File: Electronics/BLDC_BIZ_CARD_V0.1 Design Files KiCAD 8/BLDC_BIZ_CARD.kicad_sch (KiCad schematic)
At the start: 82 parts, among them J1 BATTERY, J11 A1+, J12 A1-, J13 A2+, J14 A2-, J15 B1+, J16 B1-, J17 B2+, J18 B2-, J19 C1+, J2 Conn_01x06_SERIAL_PROG_HEADER, J20 C1-, J21 C2+, J22 C2-, J4 Conn_01x04, J5 Conn_02x03_Odd_Even_ISP, J6 Conn_01x02_MOTOR_POWER, J8 Conn_01x03, J9 Conn_01x04, Q1 Q_PMOS_GSD, Q2 Q_NMOS_GSD, Q21 Q_PMOS_GSD, Q3 Q_PMOS_GSD, Q4 Q_NMOS_GSD, Q5 Q_PMOS_GSD, Q6 Q_NMOS_GSD, SW1 SK12D07L4B, U1 ATmega328PB-A, X1 SAO_Header, X2 QWIIC, Y1 20MHz 15pF Resonator

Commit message: Rotate ISP port on schematic to match board orientation.
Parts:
- J2: value Conn_01x06_SERIAL_PROG_HEADER -> Conn_01x06_SER_PROG
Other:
- note added: "AVR ISP PROGRAM"
- note added: "KEY AT PIN 3 KEY AT TOP FRONT SIDE OF PCB"
- note removed: "ISP PROGRAM"
- note removed: "KEY AT PIN 3"
- moved on the sheet: C5, J2, J5, J9

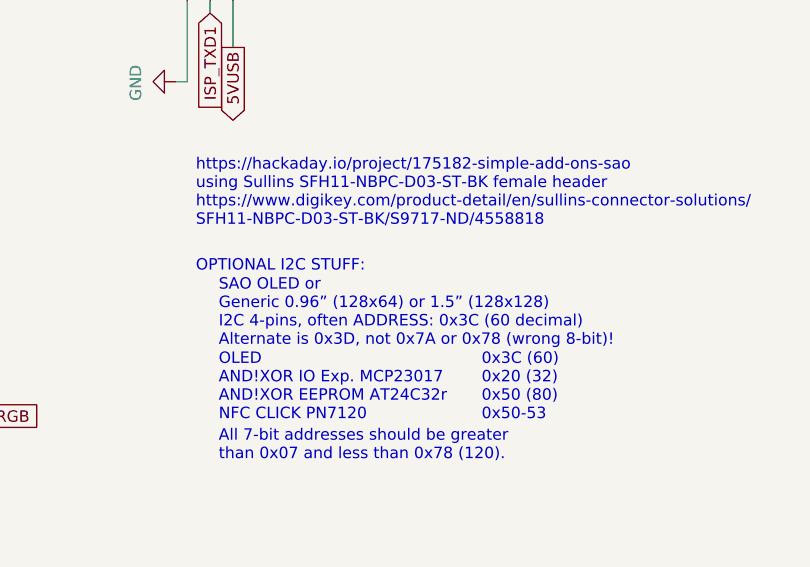
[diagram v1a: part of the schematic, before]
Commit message: Increase start-up LED color durations, add schematic OLED note
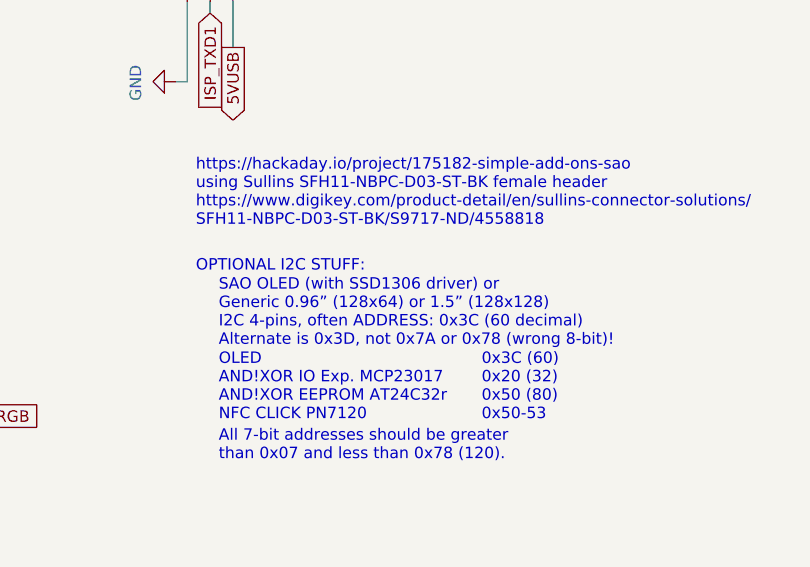
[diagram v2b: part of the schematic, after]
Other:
- note added: "SAO OLED (with SSD1306 driver) or Generic 0.96” (128x64) or 1.5” (128x128) I2C 4-pins, often ADDRESS: 0x3C (60 decimal) Alternate is 0x3D, not 0x7A or 0x78 (wrong 8-bit)!"
- note removed: "SAO OLED or Generic 0.96” (128x64) or 1.5” (128x128) I2C 4-pins, often ADDRESS: 0x3C (60 decimal) Alternate is 0x3D, not 0x7A or 0x78 (wrong 8-bit)!"
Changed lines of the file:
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@@
 		)
 	)
-	(text "SAO OLED or\nGeneric 0.96” (128x64) or 1.5” (128x128)\nI2C 4-pins, often ADDRESS: 0x3C (60 decimal)\nAlternate is 0x3D, not 0x7A or 0x78 (wrong 8-bit)!"
+	(text "SAO OLED (with SSD1306 driver) or\nGeneric 0.96” (128x64) or 1.5” (128x128)\nI2C 4-pins, often ADDRESS: 0x3C (60 decimal)\nAlternate is 0x3D, not 0x7A or 0x78 (wrong 8-bit)!"
 		(exclude_from_sim no)
 		(at 81.915 248.285 0)

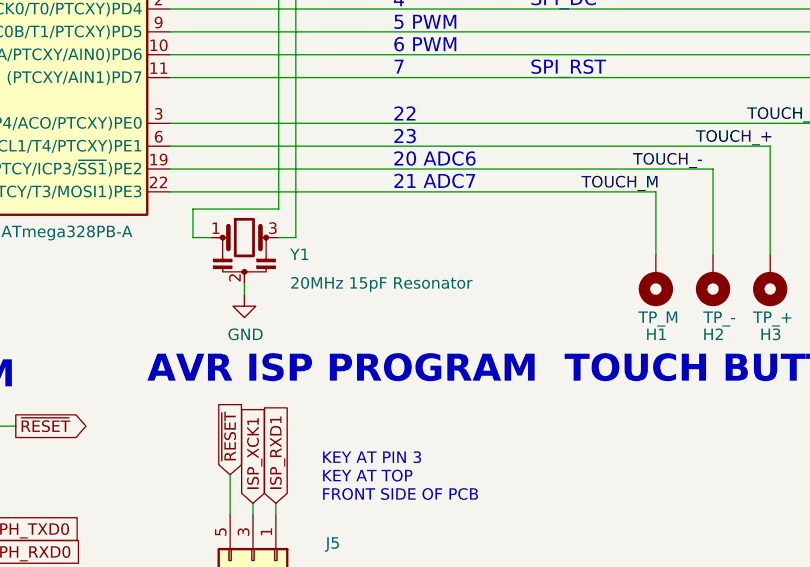
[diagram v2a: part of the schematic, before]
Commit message: Add Mech. and Elec. BOMs
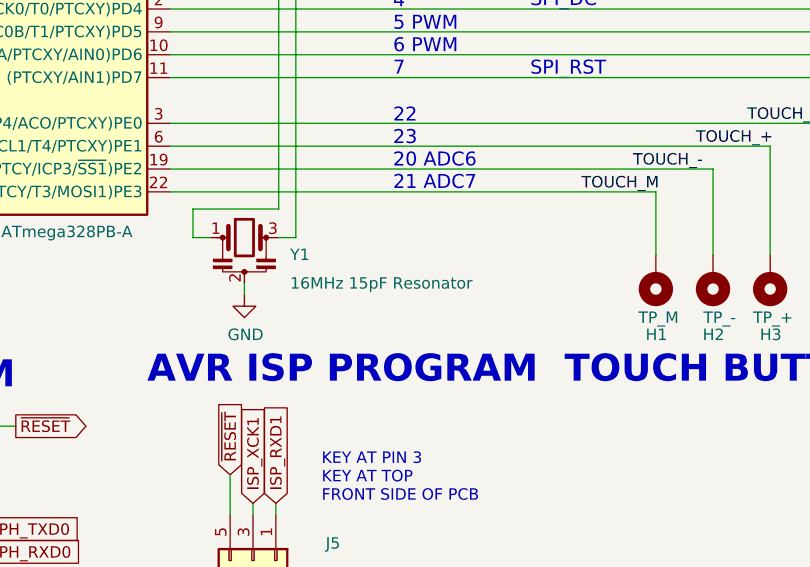
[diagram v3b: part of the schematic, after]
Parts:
- C1, C11, C12: Digi-Key_PN (none) -> 490-13970-1-ND; MPN (none) -> GRM31CR60J227ME11L
- C2: Digi-Key_PN (none) -> 1276-6472-1-ND; MPN (none) -> CL21B106KOQNNNG
- C3, C4, C5, C7: Digi-Key_PN (none) -> 1276-2922-1-ND; MPN (none) -> CL21B104KAFNNNE
- Q1, Q3, Q5: MPN (none) -> DMP2066LSN-7
- Q2, Q4, Q6: MPN NVTR4503NT1G -> DMN2020LSN-7
- Q21: MPN SL3401A-TP -> DMP2066LSN-7
- R1, R2, R3, R4, R41, R42, R43, R5, R6: Digi-Key_PN (none) -> 2019-RK73H2ATTD1001FCT-ND; MPN (none) -> RK73H2ATTD1001F
- R10, R11, R12, R13, R8, R9: MPN (none) -> RK73H2ATTD4700F
- R21, R7: Digi-Key_PN (none) -> 2019-RK73H2ATTD1002FCT-ND; MPN (none) -> RK73H2ATTD1002F
- R30, R31: Digi-Key_PN (none) -> 2019-RK73H2ATTD1201FCT-ND; MPN (none) -> RK73H2ATTD1201F
- R32, R33: Digi-Key_PN (none) -> 2019-RK73H2ATTD68R0FCT-ND; MPN (none) -> RK73H2ATTD68R0F
- U1: MPN (none) -> ATMEGA328PB-AU
- X1: MPN SFH11-NBPC-D03-ST-BK -> SFH11-NBPC-D03-ST-BK
- Y1: value 20MHz 15pF Resonator -> 16MHz 15pF Resonator; Digi-Key_PN 490-17955-1-ND -> 490-17950-1-ND; MPN (none) -> CSTNE16M0V53Z000R0
